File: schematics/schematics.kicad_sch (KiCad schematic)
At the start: 25 parts, among them M1 Motor_Servo, SW1 Reset, U1 74ACT244, U15 Dist_SW, U16 Branch_Slide, U3 Distance_Sensor, U4 PIC32MX170F256B

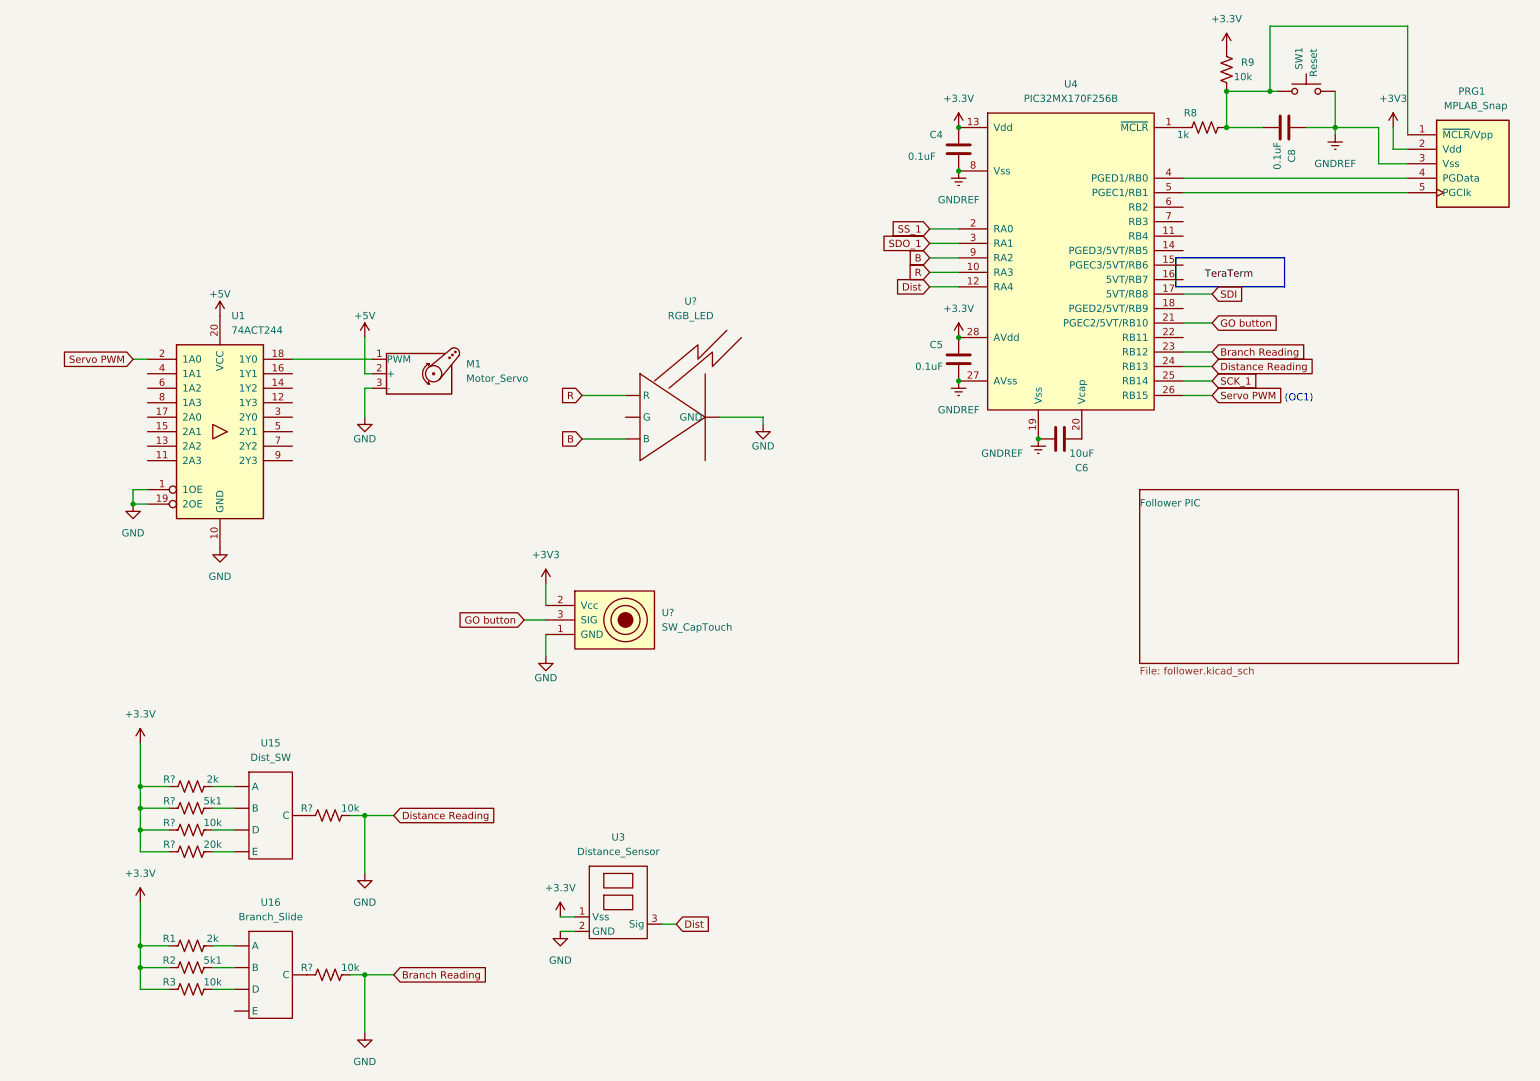
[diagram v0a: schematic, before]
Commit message: Update KiCad with new circuits, add screenshots for the website
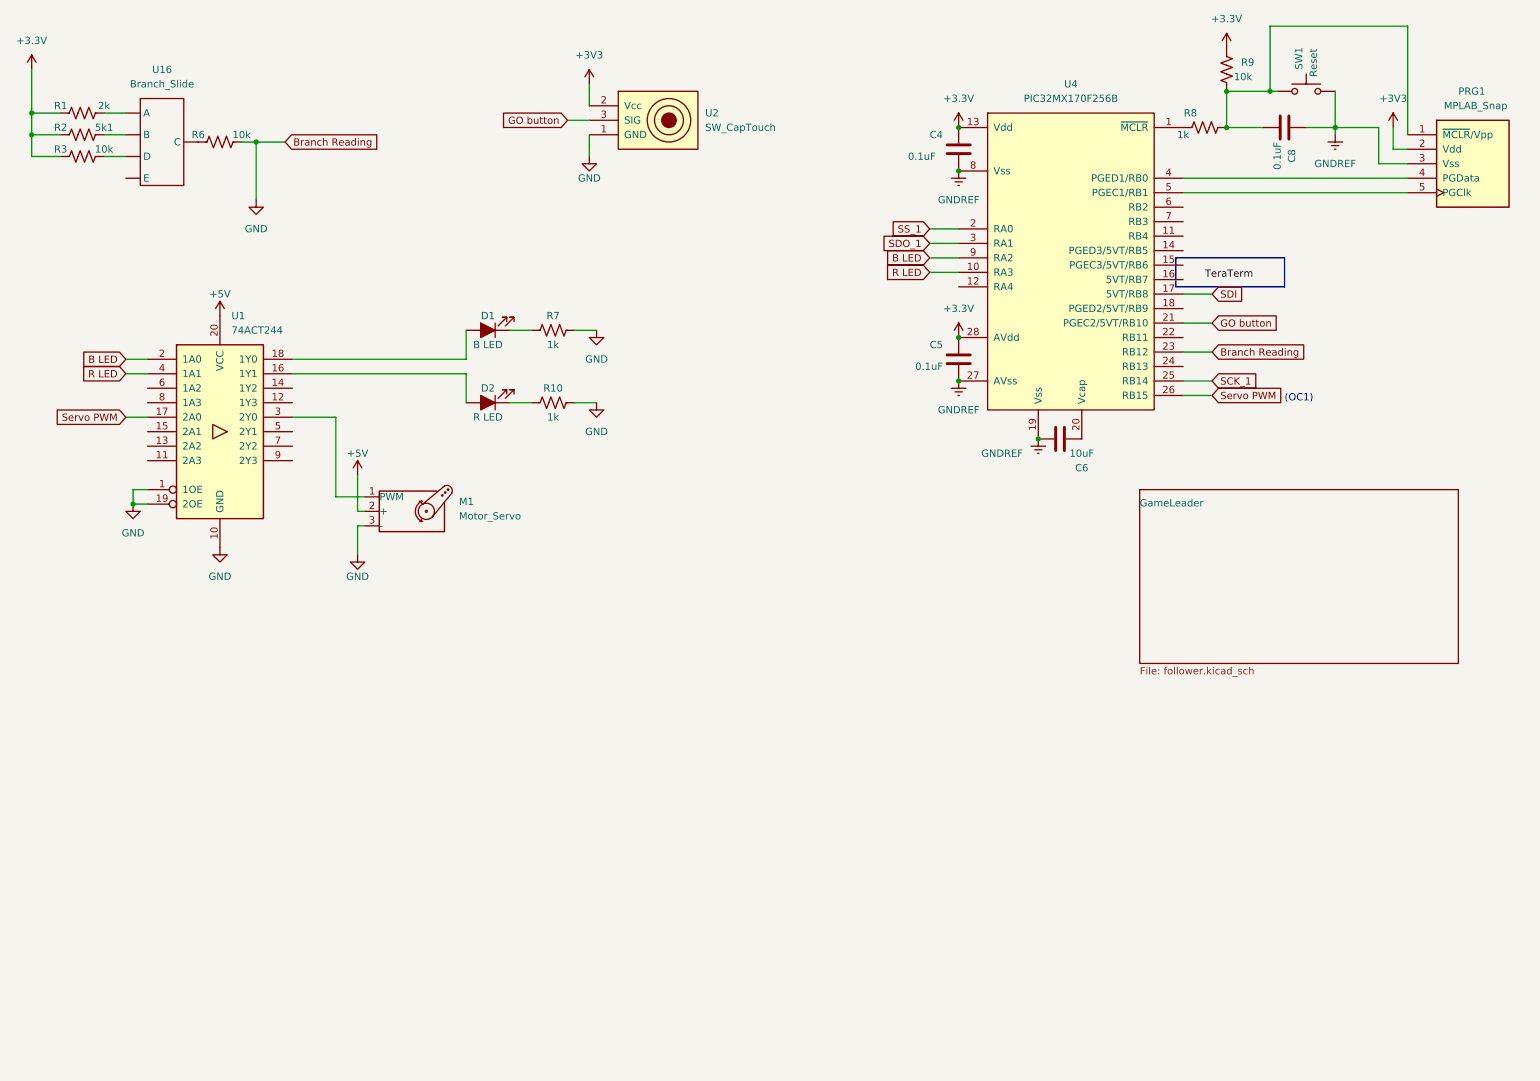
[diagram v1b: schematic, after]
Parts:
- removed R? (x2): 10k, symbol 218 spdl:Res1
- removed R?: 2k, symbol 218 spdl:Res1
- removed R?: 5k1, symbol 218 spdl:Res1
- removed R?: 20k, symbol 218 spdl:Res1
- removed U15: Dist_SW, symbol Custom_Library:Slide_SW
- removed U3: Distance_Sensor, symbol Custom_Library:Distance_Sensor
- removed U?: RGB_LED, symbol custom:RGB_LED
- added D1: B LED, symbol 218 spdl:LED
- added D2: R LED, symbol 218 spdl:LED
- added R10, R7: 1k, symbol 218 spdl:Res1
- gave numbers to parts that had none: 2
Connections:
- net R is gone; now on net R LED: U4.10 (RA3)
- net GND: now also R10.2, R7.2; no longer U4.24 (RB13)
- net Servo PWM: now also U1.17 (2A0); no longer U1.2 (1A0)
- net at U1.16 (1Y1): now also D2.2 (A)
- net at U1.18 (1Y0): now also D1.2 (A); no longer M1.1 (PWM)
- net at U1.3 (2Y0): now also M1.1 (PWM)
- net R LED: now reaches U1.4 (1A1)
- net B renamed B LED
- net B LED: now also U1.2 (1A0)
- net Dist: no longer names the net of U4.12 (RA4)
- new net: D1.1 (K), R7.1
- new net: D2.1 (K), R10.1
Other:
- sheet Follower PIC renamed GameLeader
- moved on the sheet: M1, R1, R2, R3, R6, U16, U2

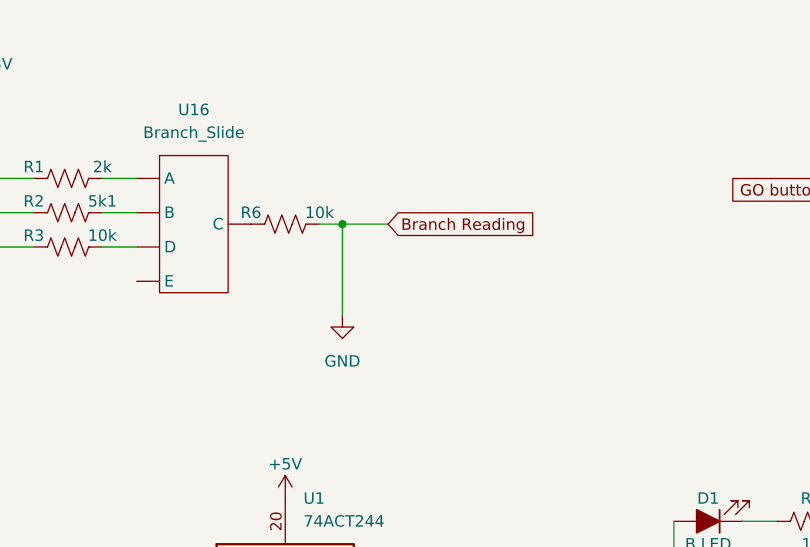
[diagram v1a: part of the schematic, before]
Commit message: Update KiCAD and CAD
* Moved input line to PIC for branch and distance switch circuits
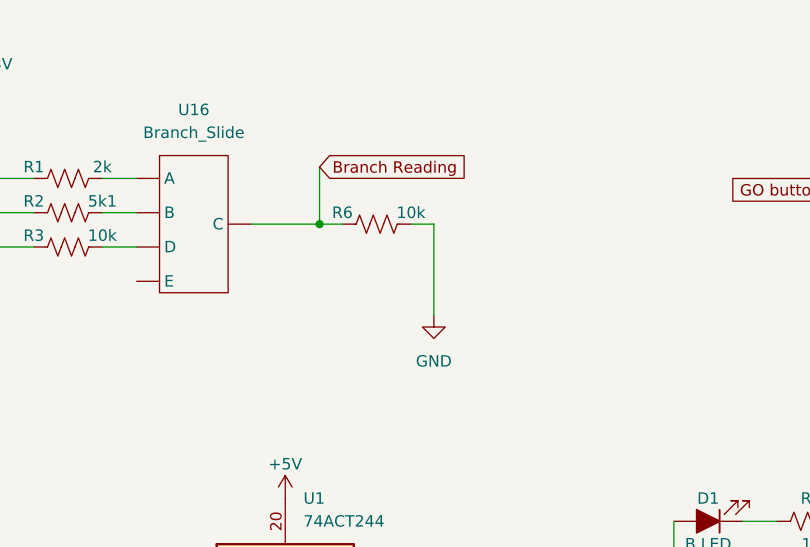
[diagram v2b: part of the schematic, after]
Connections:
- net GND: no longer U4.23 (RB12)
- net Branch Reading: now reaches R6.1, U16. (E)
- net Branch Reading: now also U4.23 (RB12)
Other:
- moved on the sheet: R6
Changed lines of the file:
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@@
   (junction (at 241.3 26.67) (diameter 0) (color 0 0 0 0)
   )
-  (junction (at 63.5 35.56) (diameter 0) (color 0 0 0 0)
-  )
   (junction (at 186.69 33.02) (diameter 0) (color 0 0 0 0)
   )
@@
   (junction (at 252.73 33.02) (diameter 0) (color 0 0 0 0)
   )
+  (junction (at 60.96 35.56) (diameter 0) (color 0 0 0 0)
+  )
   (junction (at 41.91 99.06) (diameter 0) (color 0 0 0 0)
   )
@@
     (stroke (width 0) (type default) (color 0 0 0 0))
   )
-  (wire (pts (xy 63.5 35.56) (xy 68.58 35.56))
-    (stroke (width 0) (type default) (color 0 0 0 0))
-  )
   (wire (pts (xy 265.43 34.29) (xy 265.43 15.24))
     (stroke (width 0) (type default) (color 0 0 0 0))
   )
-  (wire (pts (xy 60.96 35.56) (xy 63.5 35.56))
-    (stroke (width 0) (type default) (color 0 0 0 0))
-  )
   (wire (pts (xy 41.91 99.06) (xy 44.45 99.06))
     (stroke (width 0) (type default) (color 0 0 0 0))
@@
     (stroke (width 0) (type default) (color 0 0 0 0))
   )
+  (wire (pts (xy 60.96 35.56) (xy 53.34 35.56))
+    (stroke (width 0) (type default) (color 0 0 0 0))
+  )
   (wire (pts (xy 262.89 33.02) (xy 262.89 36.83))
     (stroke (width 0) (type default) (color 0 0 0 0))
@@
     (stroke (width 0) (type default) (color 0 0 0 0))
   )
+  (wire (pts (xy 63.5 35.56) (xy 60.96 35.56))
+    (stroke (width 0) (type default) (color 0 0 0 0))
+  )
   (wire (pts (xy 119.38 68.58) (xy 123.19 68.58))
     (stroke (width 0) (type default) (color 0 0 0 0))
@@
     (stroke (width 0) (type default) (color 0 0 0 0))
   )
+  (wire (pts (xy 60.96 29.21) (xy 60.96 35.56))
+    (stroke (width 0) (type default) (color 0 0 0 0))
+  )
   (polyline (pts (xy 224.79 60.96) (xy 243.84 60.96))
     (stroke (width 0) (type default) (color 0 0 0 0))
@@
     (stroke (width 0) (type default) (color 0 0 0 0))
   )
-  (wire (pts (xy 63.5 35.56) (xy 63.5 45.72))
+  (wire (pts (xy 73.66 35.56) (xy 73.66 45.72))
     (stroke (width 0) (type default) (color 0 0 0 0))
   )
@@
   )
   (wire (pts (xy 233.68 26.67) (xy 233.68 33.02))
+    (stroke (width 0) (type default) (color 0 0 0 0))
+  )
+  (wire (pts (xy 71.12 35.56) (xy 73.66 35.56))
     (stroke (width 0) (type default) (color 0 0 0 0))
   )
@@
     )
   )
-  (global_label "Branch Reading" (shape input) (at 68.58 35.56 0) (fields_autoplaced)
+  (global_label "Branch Reading" (shape input) (at 60.96 29.21 0) (fields_autoplaced)
     (effects (font (size 1.27 1.27)) (justify left))
-    (property "Intersheet References" "${INTERSHEET_REFS}" (id 0) (at 86.1121 35.4806 0)
+    (property "Intersheet References" "${INTERSHEET_REFS}" (id 0) (at 78.4921 29.1306 0)
       (effects (font (size 1.27 1.27)) (justify left) hide)
     )
@@
     (pin "1")
   )
-  (symbol (lib_id "power:GND") (at 63.5 45.72 0) (unit 1)
-    (in_bom yes) (on_board yes) (fields_autoplaced)
-    (property "Reference" "#PWR016" (id 0) (at 63.5 52.07 0)
-      (effects (font (size 1.27 1.27)) hide)
-    )
-    (property "Value" "GND" (id 1) (at 63.5 50.8 0))
-    (property "Footprint" "" (id 2) (at 63.5 45.72 0)
-      (effects (font (size 1.27 1.27)) hide)
-    )
-    (property "Datasheet" "" (id 3) (at 63.5 45.72 0)
+  (symbol (lib_id "power:GND") (at 73.66 45.72 0) (unit 1)
+    (in_bom yes) (on_board yes) (fields_autoplaced)
+    (property "Reference" "#PWR016" (id 0) (at 73.66 52.07 0)
+      (effects (font (size 1.27 1.27)) hide)
+    )
+    (property "Value" "GND" (id 1) (at 73.66 50.8 0))
+    (property "Footprint" "" (id 2) (at 73.66 45.72 0)
+      (effects (font (size 1.27 1.27)) hide)
+    )
+    (property "Datasheet" "" (id 3) (at 73.66 45.72 0)
       (effects (font (size 1.27 1.27)) hide)
     )
@@
     (pin "1")
   )
-  (symbol (lib_id "218 spdl:Res1") (at 57.15 35.56 90) (unit 1)
-    (in_bom yes) (on_board yes)
-    (property "Reference" "R6" (id 0) (at 53.34 34.29 90))
-    (property "Value" "10k" (id 1) (at 60.96 34.29 90))
-    (property "Footprint" "" (id 2) (at 57.404 34.544 90)
-      (effects (font (size 1.27 1.27)) hide)
-    )
-    (property "Datasheet" "" (id 3) (at 57.15 35.56 0)
-      (effects (font (size 1.27 1.27)) hide)
-    )
+  (symbol (lib_id "218 spdl:Res1") (at 67.31 35.56 90) (unit 1)
+    (in_bom yes) (on_board yes)
+    (property "Reference" "R6" (id 0) (at 63.5 34.29 90))
+    (property "Value" "10k" (id 1) (at 71.12 34.29 90))
+    (property "Footprint" "" (id 2) (at 67.564 34.544 90)
+      (effects (font (size 1.27 1.27)) hide)
+    )
+    (property "Datasheet" "" (id 3) (at 67.31 35.56 0)
+      (effects (font (size 1.27 1.27)) hide)
+    )
